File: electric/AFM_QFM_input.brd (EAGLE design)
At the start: 64.4 x 55.9 mm, 31 parts, among them U1 AD9833BRM, U2 LM339D, U3 LM324KAD, U4 SN74LVC1G86DCKRG4, Y1 OSCILLATORSMD-5X3

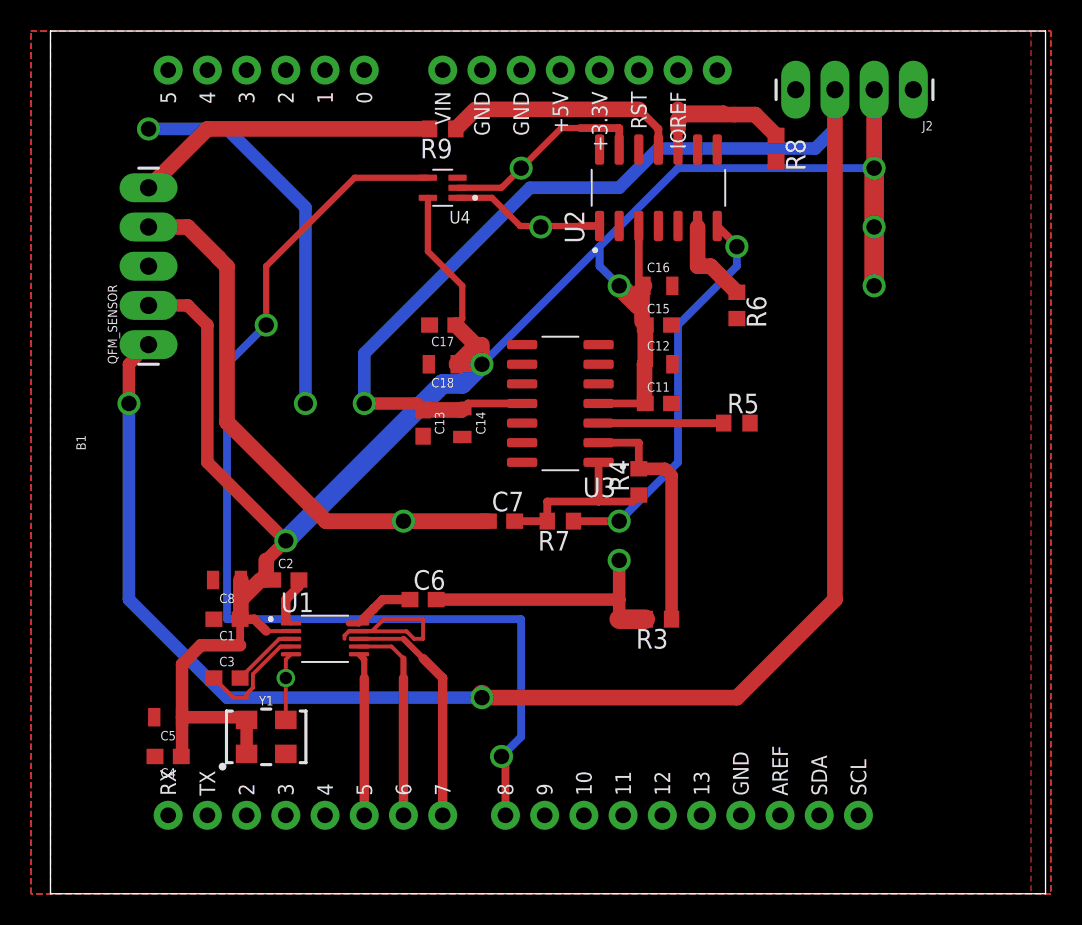
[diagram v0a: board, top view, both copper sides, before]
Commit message: Updated to boards. Changes reflects fixes needed to PCBWay boards
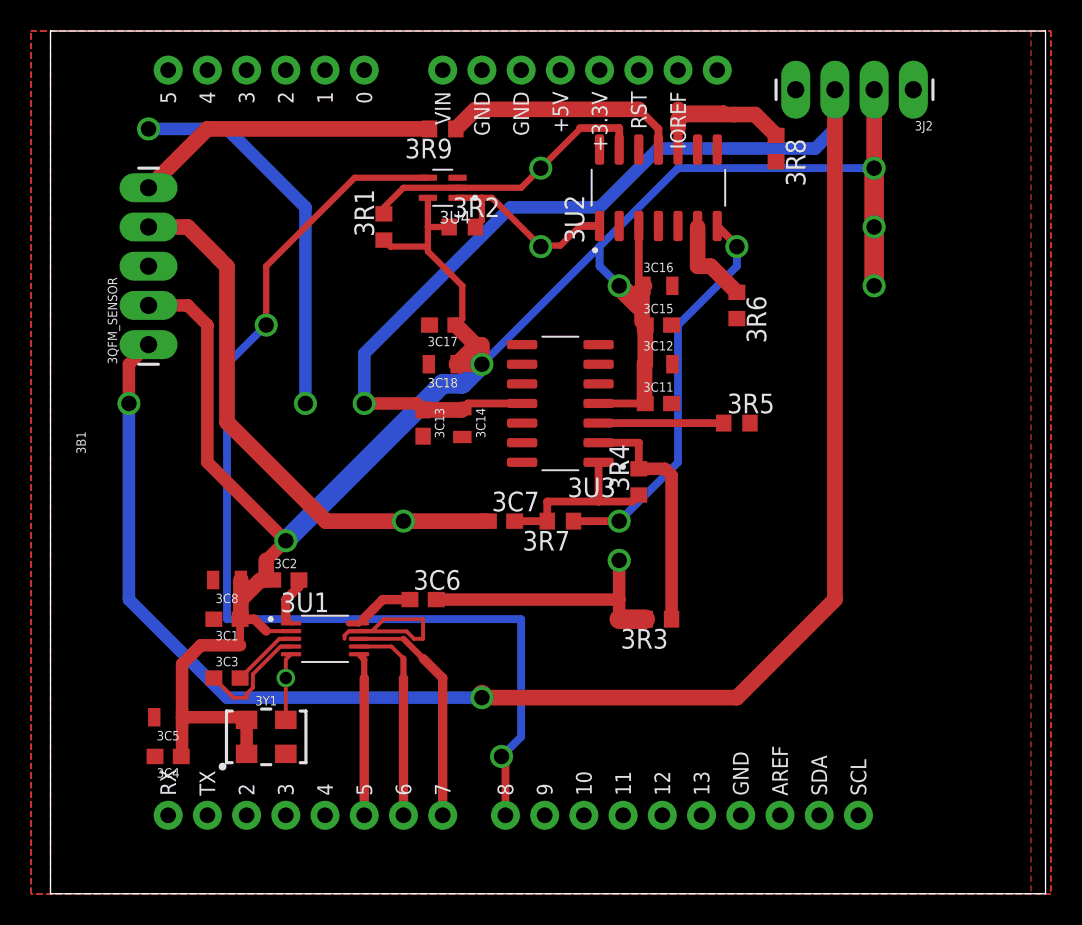
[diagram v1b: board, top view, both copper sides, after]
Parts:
- added 3R1, 3R2: 5.6k, rcl:R0603
- 3R6: value 5,6k -> 5.6k
- renumbered B1 to 3B1, C1 to 3C1, C11 to 3C11, C12 to 3C12, C13 to 3C13, C14 to 3C14, C15 to 3C15, C16 to 3C16, C17 to 3C17, C18 to 3C18, C2 to 3C2, C3 to 3C3, C4 to 3C4, C5 to 3C5, C6 to 3C6, C7 to 3C7, C8 to 3C8, J2 to 3J2, QFM_SENSOR to 3QFM_SENSOR, R3 to 3R3, R4 to 3R4, R5 to 3R5, R6 to 3R6, R7 to 3R7, R8 to 3R8, R9 to 3R9, U1 to 3U1, U2 to 3U2, U3 to 3U3, U4 to 3U4, Y1 to 3Y1
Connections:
- net N$16: now also 3R2.2
- net N$21: now also 3R1.2
- net VDD3: now also 3R1.1, 3R2.1
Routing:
- net N$21: track 13.5 -> 18.8 mm
- net VDD3: track 157.3 -> 161.7 mm
- net N$16: track 10.0 -> 13.1 mm
